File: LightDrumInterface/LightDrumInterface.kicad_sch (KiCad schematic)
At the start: 57 parts, among them J1 Conn_01x04_Male, J2 DEBUG-CONN, J3 Conn_01x04_Male, J4 PWR-CONN, J5 0525593652, J6 0541323662, SW1 RESET-SW, U1 STP16CP05, U2 TPL0401B-10-Q1, U3 74AUP2G04, U4 PC817

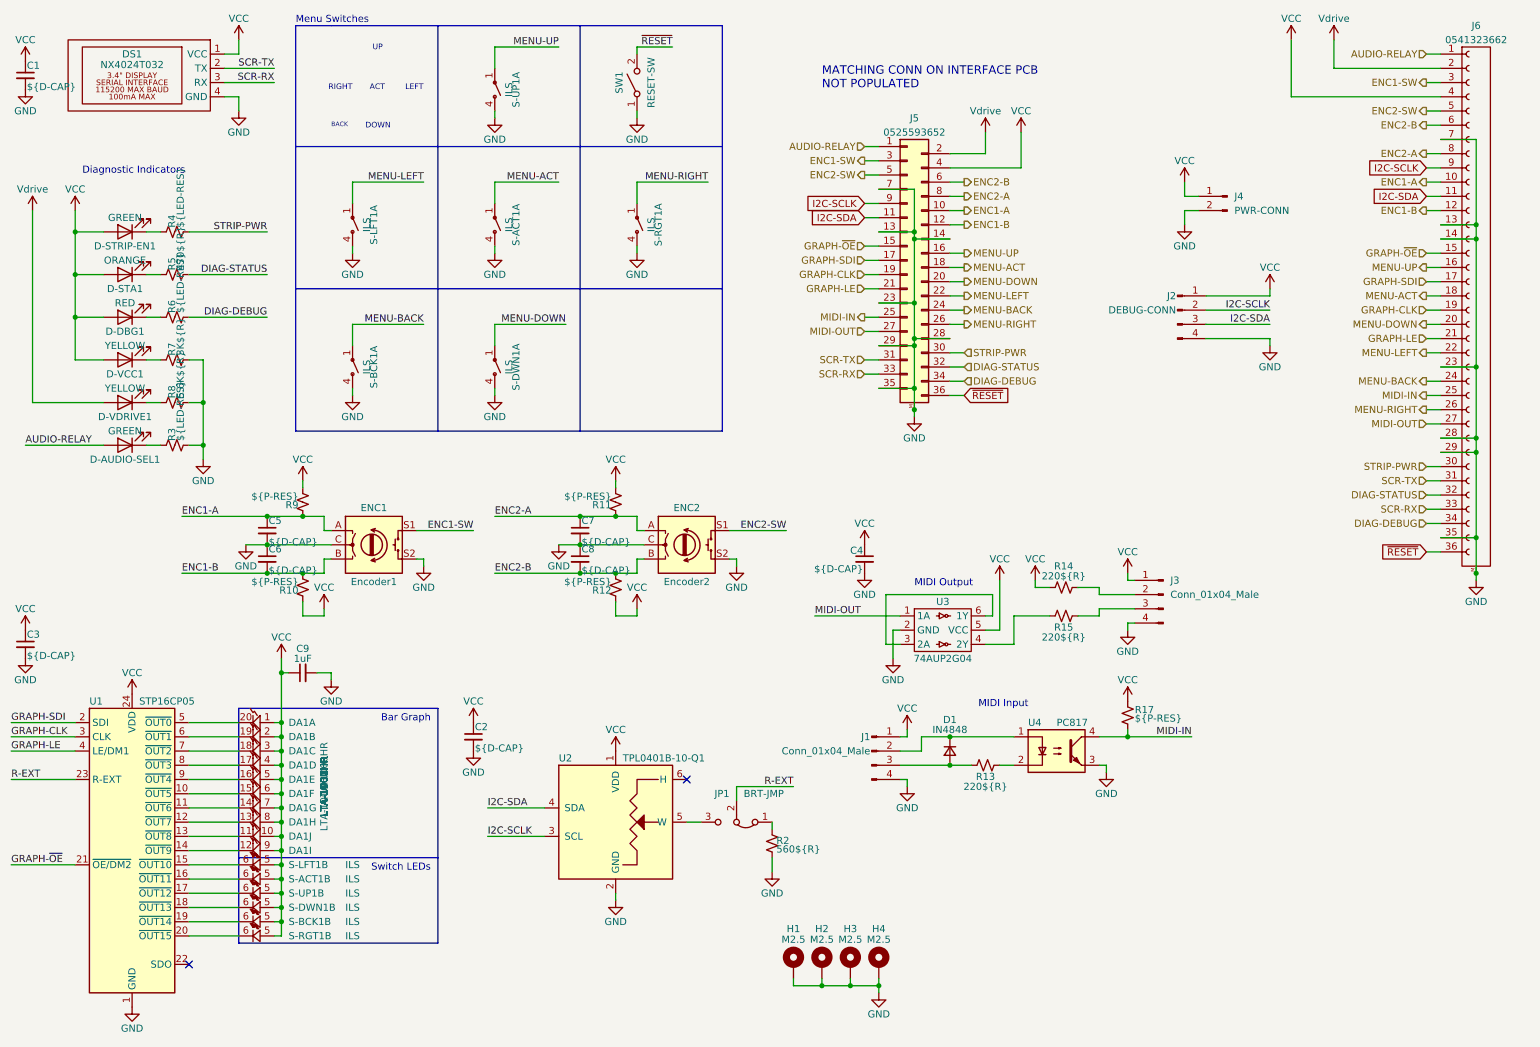
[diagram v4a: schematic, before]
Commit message: Replace with smaller case (WIP)
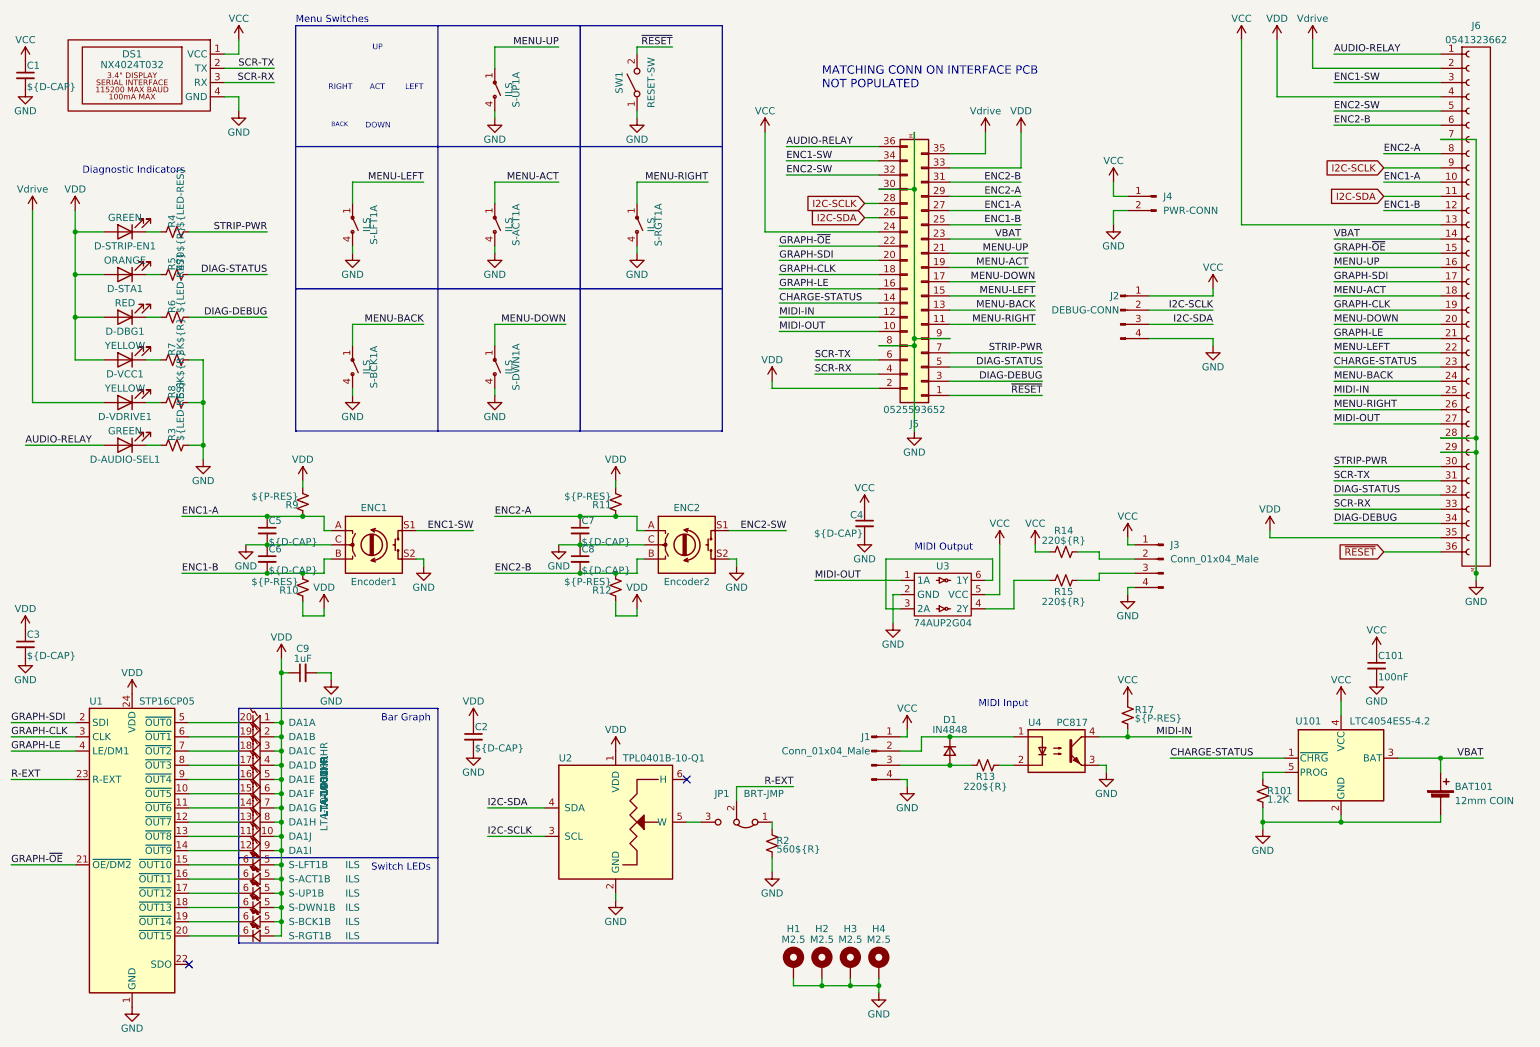
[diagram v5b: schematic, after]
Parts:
- added BAT101: 12mm COIN, Battery:BatteryHolder_Keystone_3000_1x12mm, symbol Device:Battery_Cell
- added C101: 100nF, Capacitor_SMD:C_0603_1608Metric, symbol Device:C_Small
- added R101: 1.2K, Resistor_SMD:R_0603_1608Metric, symbol Device:R_Small_US
- added U101: LTC4054ES5-4.2, Package_TO_SOT_SMD:TSOT-23-5, symbol Battery_Management:LTC4054ES5-4.2
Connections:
- net AUDIO-RELAY: now also J5.36 (Pin_36); no longer J5.1 (Pin_1)
- net DIAG-DEBUG: now also J5.3 (Pin_3); no longer J5.34 (Pin_34)
- net DIAG-STATUS: now also J5.5 (Pin_5); no longer J5.32 (Pin_32)
- net ENC1-A: now also J5.27 (Pin_27); no longer J5.10 (Pin_10)
- net ENC1-B: now also J5.25 (Pin_25); no longer J5.12 (Pin_12)
- net ENC1-SW: now also J5.34 (Pin_34); no longer J5.3 (Pin_3)
- net ENC2-A: now also J5.29 (Pin_29); no longer J5.8 (Pin_8)
- net ENC2-B: now also J5.31 (Pin_31); no longer J5.6 (Pin_6)
- net ENC2-SW: now also J5.32 (Pin_32); no longer J5.5 (Pin_5)
- net GND: now also J5.30 (Pin_30), J5.8 (Pin_8), J5.9 (Pin_9), BAT101.2 (-), C101.2, R101.2, U101.2 (GND); no longer J5.13 (Pin_13), J5.14 (Pin_14), J5.23 (Pin_23), J5.28 (Pin_28), J5.29 (Pin_29), J5.35 (Pin_35), J5.7 (Pin_7), J6.13 (Pin_13), J6.14 (Pin_14), J6.23 (Pin_23), J6.35 (Pin_35)
- net GRAPH-CLK: now also J5.18 (Pin_18); no longer J5.19 (Pin_19)
- net GRAPH-LE: now also J5.16 (Pin_16); no longer J5.21 (Pin_21)
- net GRAPH-SDI: now also J5.20 (Pin_20); no longer J5.17 (Pin_17)
- net GRAPH-~{OE}: now also J5.22 (Pin_22); no longer J5.15 (Pin_15)
- net I2C-SCLK: now also J5.28 (Pin_28); no longer J5.9 (Pin_9)
- net I2C-SDA: now also J5.26 (Pin_26); no longer J5.11 (Pin_11)
- net MENU-ACT: now also J5.19 (Pin_19); no longer J5.18 (Pin_18)
- net MENU-BACK: now also J5.13 (Pin_13); no longer J5.24 (Pin_24)
- net MENU-DOWN: now also J5.17 (Pin_17); no longer J5.20 (Pin_20)
- net MENU-LEFT: now also J5.15 (Pin_15); no longer J5.22 (Pin_22)
- net MENU-RIGHT: now also J5.11 (Pin_11); no longer J5.26 (Pin_26)
- net MENU-UP: now also J5.21 (Pin_21); no longer J5.16 (Pin_16)
- net MIDI-IN: now also J5.12 (Pin_12); no longer J5.25 (Pin_25)
- net MIDI-OUT: now also J5.10 (Pin_10); no longer J5.27 (Pin_27)
- net SCR-RX: now also J5.4 (Pin_4); no longer J5.33 (Pin_33)
- net SCR-TX: now also J5.6 (Pin_6); no longer J5.31 (Pin_31)
- net STRIP-PWR: now also J5.7 (Pin_7); no longer J5.30 (Pin_30)
- net VCC: now also J5.24 (Pin_24), J6.13 (Pin_13), C101.1, U101.4 (VCC); no longer C2.1, C3.1, C9.1, D-DBG1.2 (A), D-STA1.2 (A), D-STRIP-EN1.2 (A), D-VCC1.2 (A), DA1.1, DA1.10, DA1.2, DA1.3, DA1.4, DA1.5, DA1.6, DA1.7, DA1.8, DA1.9, J5.4 (Pin_4), J6.4 (Pin_4), R10.1, R11.2, R12.1, R9.2, S-ACT1.5, S-BCK1.5, S-DWN1.5, S-LFT1.5, S-RGT1.5, S-UP1.5, U1.24 (VDD), U2.1 (VDD)
- net Vdrive: now also J5.35 (Pin_35); no longer J5.2 (Pin_2)
- net ~{RESET}: now also J5.1 (Pin_1); no longer J5.36 (Pin_36)
- new net: R101.1, U101.5 (PROG)
- new net CHARGE-STATUS: J5.14 (Pin_14), J6.23 (Pin_23), U101.1 (~{CHRG})
- new net VBAT: BAT101.1 (+), J5.23 (Pin_23), J6.14 (Pin_14), U101.3 (BAT)
- new net VDD: C2.1, C3.1, C9.1, D-DBG1.2 (A), D-STA1.2 (A), D-STRIP-EN1.2 (A), D-VCC1.2 (A), DA1.1, DA1.10, DA1.2, DA1.3, DA1.4, DA1.5, DA1.6, DA1.7, DA1.8, DA1.9, J5.2 (Pin_2), J5.33 (Pin_33), J6.35 (Pin_35), J6.4 (Pin_4), R10.1, R11.2, R12.1, R9.2, S-ACT1.5, S-BCK1.5, S-DWN1.5, S-LFT1.5, S-RGT1.5, S-UP1.5, U1.24 (VDD), U2.1 (VDD)
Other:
- moved on the sheet: C4, J2, J3, J4, J5, R14, R15, U3

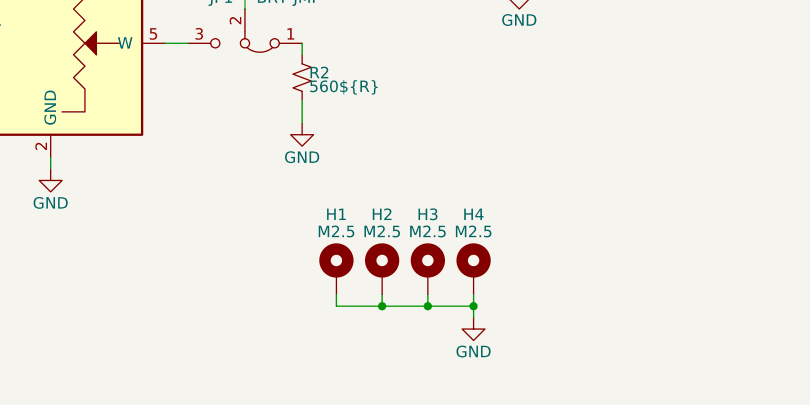
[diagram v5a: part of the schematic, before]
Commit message: Simplify analog power supply and add some routing
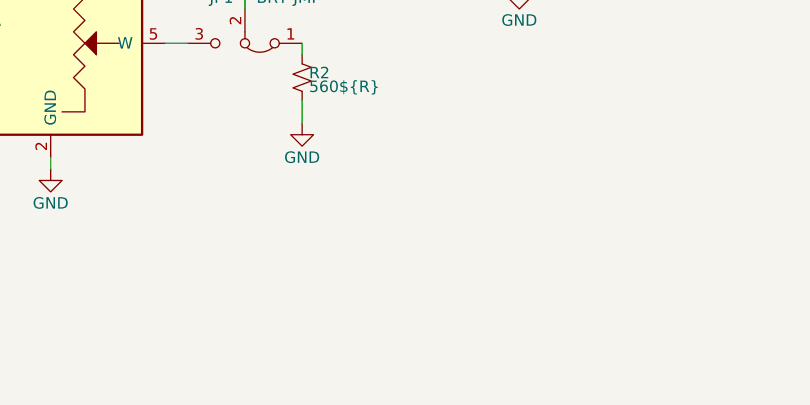
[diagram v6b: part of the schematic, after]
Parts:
- removed H1, H2, H3, H4: M2.5, MountingHole:MountingHole_2.5mm_Pad, symbol Mechanical:MountingHole_Pad
- DS1: footprint Daxxn_Displays:NX4024T032_10mm_Harness -> Daxxn_Displays:NX4024T032_10mm
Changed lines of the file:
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@@
   (junction (at 60.96 109.22) (diameter 0) (color 0 0 0 0)
   )
-  (junction (at 160.02 187.96) (diameter 0) (color 0 0 0 0)
-  )
   (junction (at 63.5 132.08) (diameter 0) (color 0 0 0 0)
   )
@@
   (junction (at 63.5 153.67) (diameter 0) (color 0 0 0 0)
   )
-  (junction (at 165.1 187.96) (diameter 0) (color 0 0 0 0)
-  )
   (junction (at 63.5 151.13) (diameter 0) (color 0 0 0 0)
   )
@@
   (junction (at 214.63 143.51) (diameter 0) (color 0 0 0 0)
   )
-  (junction (at 170.18 187.96) (diameter 0) (color 0 0 0 0)
-  )
   (junction (at 49.53 83.82) (diameter 0) (color 0 0 0 0)
   )
@@
     (stroke (width 0) (type default) (color 0 0 0 0))
   )
-  (wire (pts (xy 170.18 187.96) (xy 170.18 189.23))
-    (stroke (width 0) (type default) (color 0 0 0 0))
-  )
   (wire (pts (xy 238.76 149.86) (xy 238.76 151.13))
     (stroke (width 0) (type default) (color 0 0 0 0))
@@
     (stroke (width 0) (type default) (color 0 0 0 0))
   )
-  (wire (pts (xy 160.02 187.96) (xy 165.1 187.96))
-    (stroke (width 0) (type default) (color 0 0 0 0))
-  )
   (wire (pts (xy 251.46 26.67) (xy 270.51 26.67))
     (stroke (width 0) (type default) (color 0 0 0 0))
@@
     (stroke (width 0) (type default) (color 0 0 0 0))
   )
-  (wire (pts (xy 154.94 186.69) (xy 154.94 187.96))
-    (stroke (width 0) (type default) (color 0 0 0 0))
-  )
   (wire (pts (xy 171.45 120.65) (xy 173.99 120.65))
     (stroke (width 0) (type default) (color 0 0 0 0))
@@
     (stroke (width 0) (type default) (color 0 0 0 0))
   )
-  (wire (pts (xy 154.94 187.96) (xy 160.02 187.96))
-    (stroke (width 0) (type default) (color 0 0 0 0))
-  )
   (wire (pts (xy 205.74 115.57) (xy 209.55 115.57))
     (stroke (width 0) (type default) (color 0 0 0 0))
@@
     (stroke (width 0) (type default) (color 0 0 0 0))
   )
-  (wire (pts (xy 170.18 186.69) (xy 170.18 187.96))
-    (stroke (width 0) (type default) (color 0 0 0 0))
-  )
   (wire (pts (xy 209.55 114.3) (xy 209.55 115.57))
     (stroke (width 0) (type default) (color 0 0 0 0))
@@
     (stroke (width 0) (type default) (color 0 0 0 0))
   )
-  (wire (pts (xy 160.02 186.69) (xy 160.02 187.96))
-    (stroke (width 0) (type default) (color 0 0 0 0))
-  )
   (wire (pts (xy 39.37 60.96) (xy 41.91 60.96))
     (stroke (width 0) (type default) (color 0 0 0 0))
@@
     (stroke (width 0) (type default) (color 0 0 0 0))
   )
-  (wire (pts (xy 165.1 187.96) (xy 170.18 187.96))
-    (stroke (width 0) (type default) (color 0 0 0 0))
-  )
   (wire (pts (xy 128.27 111.76) (xy 127 111.76))
     (stroke (width 0) (type default) (color 0 0 0 0))
@@
     (stroke (width 0) (type default) (color 0 0 0 0))
   )
-  (wire (pts (xy 165.1 186.69) (xy 165.1 187.96))
-    (stroke (width 0) (type default) (color 0 0 0 0))
-  )
   (wire (pts (xy 175.26 142.24) (xy 175.26 143.51))
     (stroke (width 0) (type default) (color 0 0 0 0))
@@
     (pin "6")
   )
-  (symbol (lib_id "Mechanical:MountingHole_Pad") (at 165.1 184.15 0) (unit 1)
-    (in_bom yes) (on_board yes)
-    (property "Reference" "H3" (id 0) (at 165.1 177.8 0))
-    (property "Value" "M2.5" (id 1) (at 165.1 179.705 0))
-    (property "Footprint" "MountingHole:MountingHole_2.5mm_Pad" (id 2) (at 165.1 184.15 0)
-      (effects (font (size 1.27 1.27)) hide)
-    )
-    (property "Datasheet" "~" (id 3) (at 165.1 184.15 0)
-      (effects (font (size 1.27 1.27)) hide)
-    )
-    (pin "1")
-  )
   (symbol (lib_id "power:Vdrive") (at 247.65 19.05 0) (unit 1)
     (in_bom yes) (on_board yes)
@@
     (pin "1")
   )
-  (symbol (lib_id "power:GND") (at 170.18 189.23 0) (unit 1)
-    (in_bom yes) (on_board yes)
-    (property "Reference" "#PWR031" (id 0) (at 170.18 195.58 0)
-      (effects (font (size 1.27 1.27)) hide)
-    )
-    (property "Value" "GND" (id 1) (at 170.18 193.04 0))
-    (property "Footprint" "" (id 2) (at 170.18 189.23 0)
-      (effects (font (size 1.27 1.27)) hide)
-    )
-    (property "Datasheet" "" (id 3) (at 170.18 189.23 0)
-      (effects (font (size 1.27 1.27)) hide)
-    )
-    (pin "1")
-  )
-  (symbol (lib_id "Mechanical:MountingHole_Pad") (at 170.18 184.15 0) (unit 1)
-    (in_bom yes) (on_board yes)
-    (property "Reference" "H4" (id 0) (at 170.18 177.8 0))
-    (property "Value" "M2.5" (id 1) (at 170.18 179.705 0))
-    (property "Footprint" "MountingHole:MountingHole_2.5mm_Pad" (id 2) (at 170.18 184.15 0)
-      (effects (font (size 1.27 1.27)) hide)
-    )
-    (property "Datasheet" "~" (id 3) (at 170.18 184.15 0)
-      (effects (font (size 1.27 1.27)) hide)
-    )
-    (pin "1")
-  )
   (symbol (lib_id "Daxxn_Logic:74AUP2G04") (at 173.99 115.57 0) (unit 1)
     (in_bom yes) (on_board yes)
@@
     (property "Reference" "DS1" (id 0) (at 36.83 21.59 0))
     (property "Value" "NX4024T032" (id 1) (at 36.83 23.495 0))
-    (property "Footprint" "Daxxn_Displays:NX4024T032_10mm_Harness" (id 2) (at 36.83 17.78 0)
+    (property "Footprint" "Daxxn_Displays:NX4024T032_10mm" (id 2) (at 36.83 17.78 0)
       (effects (font (size 1.27 1.27)) hide)
     )
@@
     (pin "2")
   )
-  (symbol (lib_id "Mechanical:MountingHole_Pad") (at 154.94 184.15 0) (unit 1)
-    (in_bom yes) (on_board yes)
-    (property "Reference" "H1" (id 0) (at 154.94 177.8 0))
-    (property "Value" "M2.5" (id 1) (at 154.94 179.705 0))
-    (property "Footprint" "MountingHole:MountingHole_2.5mm_Pad" (id 2) (at 154.94 184.15 0)
-      (effects (font (size 1.27 1.27)) hide)
-    )
-    (property "Datasheet" "~" (id 3) (at 154.94 184.15 0)
-      (effects (font (size 1.27 1.27)) hide)
-    )
-    (pin "1")
-  )
   (symbol (lib_id "power:VCC") (at 55.88 19.05 0) (unit 1)
     (in_bom yes) (on_board yes)
@@
     (pin "2")
   )
-  (symbol (lib_id "Mechanical:MountingHole_Pad") (at 160.02 184.15 0) (unit 1)
-    (in_bom yes) (on_board yes)
-    (property "Reference" "H2" (id 0) (at 160.02 177.8 0))
-    (property "Value" "M2.5" (id 1) (at 160.02 179.705 0))
-    (property "Footprint" "MountingHole:MountingHole_2.5mm_Pad" (id 2) (at 160.02 184.15 0)
-      (effects (font (size 1.27 1.27)) hide)
-    )
-    (property "Datasheet" "~" (id 3) (at 160.02 184.15 0)
-      (effects (font (size 1.27 1.27)) hide)
-    )
-    (pin "1")
-  )
   (symbol (lib_id "Daxxn_Buttons:ILS") (at 58.42 171.45 0) (mirror y) (unit 2)
     (in_bom yes) (on_board yes)
@@
       (reference "#PWR030") (unit 1) (value "GND") (footprint "")
     )
-    (path "/1cefa9f7-9fb2-4a9f-89ca-522515d090c8"
-      (reference "#PWR031") (unit 1) (value "GND") (footprint "")
-    )
     (path "/bcf6a9aa-a9b9-4c9e-ac53-b5e9db30c44d"
       (reference "#PWR032") (unit 1) (value "GND") (footprint "")
@@
     )
     (path "/91f41def-a8bb-4343-8bf1-623bcd9609c4"
-      (reference "DS1") (unit 1) (value "NX4024T032") (footprint "Daxxn_Displays:NX4024T032_10mm_Harness")
+      (reference "DS1") (unit 1) (value "NX4024T032") (footprint "Daxxn_Displays:NX4024T032_10mm")
     )
     (path "/3fc7e44e-eaa5-446c-aee1-c1bf6217aff8"
@@
       (reference "ENC2") (unit 1) (value "Encoder2") (footprint "Daxxn_Switches:PEC12R")
     )
-    (path "/a87241e0-9c77-4a8b-b263-8fdfba3f8915"
-      (reference "H1") (unit 1) (value "M2.5") (footprint "MountingHole:MountingHole_2.5mm_Pad")
-    )
-    (path "/c43b9530-f844-481b-9582-de35d3a89b4b"
-      (reference "H2") (unit 1) (value "M2.5") (footprint "MountingHole:MountingHole_2.5mm_Pad")
-    )
-    (path "/06e6f57f-1ce1-4398-aac6-943a97588e35"
-      (reference "H3") (unit 1) (value "M2.5") (footprint "MountingHole:MountingHole_2.5mm_Pad")
-    )
-    (path "/2333ca33-e57a-4c68-b5ee-744c500f9da5"
-      (reference "H4") (unit 1) (value "M2.5") (footprint "MountingHole:MountingHole_2.5mm_Pad")
-    )
     (path "/0379ca40-a8b5-41c6-a6e3-6a60b06d346b"

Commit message: Remove RTC and battery
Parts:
- removed BAT101: 12mm COIN, Battery:BatteryHolder_Keystone_3000_1x12mm, symbol Device:Battery_Cell
- removed C101: 100nF, Capacitor_SMD:C_0603_1608Metric, symbol Device:C_Small
- removed R101: 1.2K, Resistor_SMD:R_0603_1608Metric, symbol Device:R_Small_US
- removed U101: LTC4054ES5-4.2, Package_TO_SOT_SMD:TSOT-23-5, symbol Battery_Management:LTC4054ES5-4.2
- J1: value Conn_01x04_Male -> MIDI-IN
- J3: value Conn_01x04_Male -> MIDI-OUT
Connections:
- net GND: now also J6.14 (Pin_14), J6.23 (Pin_23)
- net CHARGE-STATUS: no longer names the net of J5.14 (Pin_14)
- net CHARGE-STATUS: no longer J6.23 (Pin_23)
- net VBAT: no longer names the net of J5.23 (Pin_23)
- net VBAT: no longer J6.14 (Pin_14)
